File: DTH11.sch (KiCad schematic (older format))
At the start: 2 parts, among them P7 CONN_01X03

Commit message: finalizado enrutado provisional
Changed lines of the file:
@@
 $Descr User 8268 5846
 encoding utf-8
-Sheet 14 14
+Sheet 14 15
 Title ""
 Date ""
@@
 $EndDescr
 $Comp
-L +5V #PWR057
+L +5V #PWR050
 U 1 1 57993E23
 P 2150 1850
-F 0 "#PWR057" H 2150 1700 50  0001 C CNN
+F 0 "#PWR050" H 2150 1700 50  0001 C CNN
 F 1 "+5V" H 2165 2023 50  0000 C CNN
 F 2 "" H 2150 1850 50  0000 C CNN
@@
 $EndComp
 $Comp
-L GND #PWR058
+L GND #PWR051
 U 1 1 57993E44
-P 2350 3000
-F 0 "#PWR058" H 2350 2750 50  0001 C CNN
-F 1 "GND" H 2355 2827 50  0000 C CNN
-F 2 "" H 2350 3000 50  0000 C CNN
-F 3 "" H 2350 3000 50  0000 C CNN
-	1    2350 3000
+P 2350 3150
+F 0 "#PWR051" H 2350 2900 50  0001 C CNN
+F 1 "GND" H 2355 2977 50  0000 C CNN
+F 2 "" H 2350 3150 50  0000 C CNN
+F 3 "" H 2350 3150 50  0000 C CNN
+	1    2350 3150
 	1    0    0    -1
 $EndComp
@@
 6F 6A 98 BE 51 A3 46 8D 1A 35 6A D4 A8 51 A3 BF 6F 6A 98 BE 51 A3 46 8D 1A 35 6A D4 A8 51 A3 BF
 6F 6A 98 BE 51 A3 46 8D 1A 35 6A D4 A8 51 A3 BF 6F FA 7F 01 6A B6 0B 1D 9C B5 4B 53 00 00 00 00
-49 45 4E 44 AE 42 60 82 B1
+49 45 4E 44 AE 42 60 82 11
 EndData
 $EndBitmap

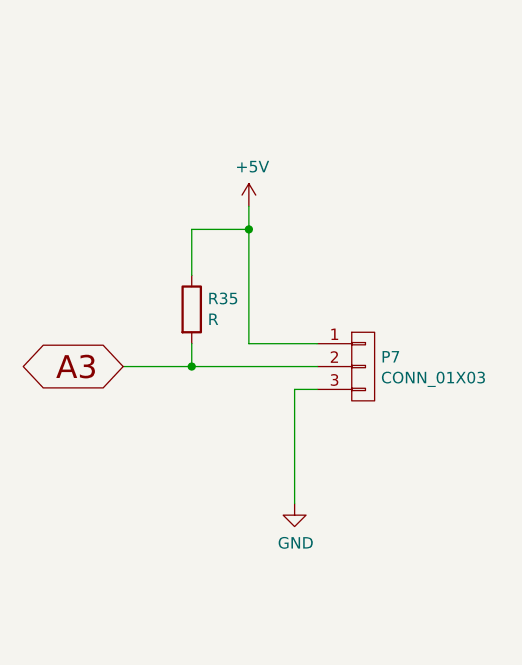
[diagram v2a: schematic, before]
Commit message: ordenar referencias de componentes
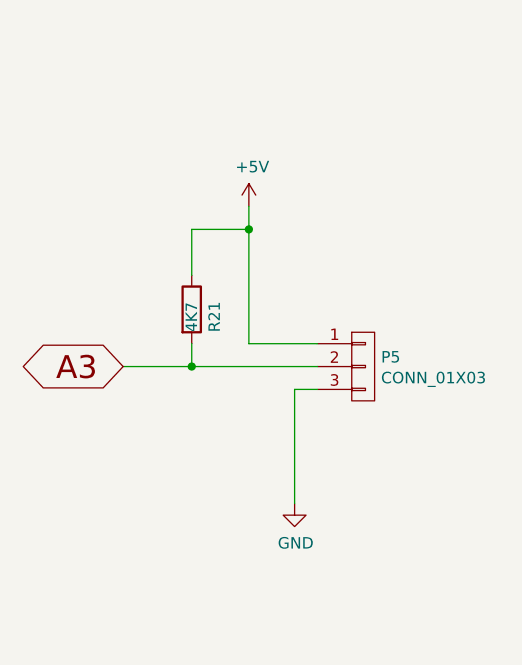
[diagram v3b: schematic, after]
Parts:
- P5: renamed from P7; Fabricante (none) -> NINIGI; Provedor (none) -> TME; Ref (none) -> ZL262-40SG; Ref_Proveedor (none) -> ZL262-40SG
- R21: renamed from R35; value R -> 4K7; Fabricante (none) -> VISHAY; Potencia (none) -> 1/8W; Provedor (none) -> TME; Ref (none) -> CRCW08054K70FKEA; Ref_Proveedor (none) -> CRCW08054K70FKEA; Tolerancia (none) -> 1%
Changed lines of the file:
@@
 $Descr User 8268 5846
 encoding utf-8
-Sheet 14 15
+Sheet 8 15
 Title ""
 Date ""
@@
 $EndDescr
 $Comp
-L +5V #PWR050
+L +5V #PWR22
 U 1 1 57993E23
 P 2150 1850
-F 0 "#PWR050" H 2150 1700 50  0001 C CNN
+F 0 "#PWR22" H 2150 1700 50  0001 C CNN
 F 1 "+5V" H 2165 2023 50  0000 C CNN
 F 2 "" H 2150 1850 50  0000 C CNN
@@
 $EndComp
 $Comp
-L GND #PWR051
+L GND #PWR23
 U 1 1 57993E44
 P 2350 3150
-F 0 "#PWR051" H 2350 2900 50  0001 C CNN
+F 0 "#PWR23" H 2350 2900 50  0001 C CNN
 F 1 "GND" H 2355 2977 50  0000 C CNN
 F 2 "" H 2350 3150 50  0000 C CNN
@@
 6F 6A 98 BE 51 A3 46 8D 1A 35 6A D4 A8 51 A3 BF 6F 6A 98 BE 51 A3 46 8D 1A 35 6A D4 A8 51 A3 BF
 6F 6A 98 BE 51 A3 46 8D 1A 35 6A D4 A8 51 A3 BF 6F FA 7F 01 6A B6 0B 1D 9C B5 4B 53 00 00 00 00
-49 45 4E 44 AE 42 60 82 11
+49 45 4E 44 AE 42 60 82 E1
 EndData
 $EndBitmap
 $Comp
-L CONN_01X03 P7
+L CONN_01X03 P5
 U 1 1 57993F2D
 P 2650 2550
-F 0 "P7" H 2728 2591 50  0000 L CNN
+F 0 "P5" H 2728 2591 50  0000 L CNN
 F 1 "CONN_01X03" H 2728 2500 50  0000 L CNN
 F 2 "Socket_Strips:Socket_Strip_Straight_1x03" H 2650 2550 50  0001 C CNN
 F 3 "" H 2650 2550 50  0000 C CNN
+F 4 "NINIGI" H 2650 2550 60  0001 C CNN "Fabricante"
+F 5 "ZL262-40SG" H 2650 2550 60  0001 C CNN "Ref"
+F 6 "~" H 2650 2550 60  0001 C CNN "Potencia"
+F 7 "~" H 2650 2550 60  0001 C CNN "Tolerancia"
+F 8 "TME" H 2650 2550 60  0001 C CNN "Provedor"
+F 9 "ZL262-40SG" H 2650 2550 60  0001 C CNN "Ref_Proveedor"
 	1    2650 2550
 	1    0    0    -1
@@
 	1900 1950 1900 2150
 $Comp
-L R R35
+L R R21
 U 1 1 57993FBE
 P 1900 2300
-F 0 "R35" H 1970 2346 50  0000 L CNN
-F 1 "R" H 1970 2255 50  0000 L CNN
+F 0 "R21" V 2000 2200 50  0000 L CNN
+F 1 "4K7" V 1900 2200 50  0000 L CNN
 F 2 "Resistors_SMD:R_0805" V 1830 2300 50  0001 C CNN
 F 3 "" H 1900 2300 50  0000 C CNN
+F 4 "VISHAY" H 1900 2300 60  0001 C CNN "Fabricante"
+F 5 "CRCW08054K70FKEA" H 1900 2300 60  0001 C CNN "Ref"
+F 6 "1/8W" H 1900 2300 60  0001 C CNN "Potencia"
+F 7 "1%" H 1900 2300 60  0001 C CNN "Tolerancia"
+F 8 "TME" H 1900 2300 60  0001 C CNN "Provedor"
+F 9 "CRCW08054K70FKEA" H 1900 2300 60  0001 C CNN "Ref_Proveedor"
 	1    1900 2300
 	1    0    0    -1

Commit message: cambiados encoder y potenciometro
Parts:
- R21: footprint Resistors_SMD:R_0805 -> Resistencias:R_0805
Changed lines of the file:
@@
 $EndDescr
 $Comp
-L +5V #PWR22
+L +5V #PWR024
 U 1 1 57993E23
 P 2150 1850
-F 0 "#PWR22" H 2150 1700 50  0001 C CNN
+F 0 "#PWR024" H 2150 1700 50  0001 C CNN
 F 1 "+5V" H 2165 2023 50  0000 C CNN
 F 2 "" H 2150 1850 50  0000 C CNN
@@
 $EndComp
 $Comp
-L GND #PWR23
+L GND #PWR025
 U 1 1 57993E44
 P 2350 3150
-F 0 "#PWR23" H 2350 2900 50  0001 C CNN
+F 0 "#PWR025" H 2350 2900 50  0001 C CNN
 F 1 "GND" H 2355 2977 50  0000 C CNN
 F 2 "" H 2350 3150 50  0000 C CNN
@@
 6F 6A 98 BE 51 A3 46 8D 1A 35 6A D4 A8 51 A3 BF 6F 6A 98 BE 51 A3 46 8D 1A 35 6A D4 A8 51 A3 BF
 6F 6A 98 BE 51 A3 46 8D 1A 35 6A D4 A8 51 A3 BF 6F FA 7F 01 6A B6 0B 1D 9C B5 4B 53 00 00 00 00
-49 45 4E 44 AE 42 60 82 91
+49 45 4E 44 AE 42 60 82 C1
 EndData
 $EndBitmap
@@
 F 0 "R21" V 2000 2200 50  0000 L CNN
 F 1 "4K7" V 1900 2200 50  0000 L CNN
-F 2 "Resistors_SMD:R_0805" V 1830 2300 50  0001 C CNN
+F 2 "Resistencias:R_0805" V 1830 2300 50  0001 C CNN
 F 3 "" H 1900 2300 50  0000 C CNN
 F 4 "VISHAY" H 1900 2300 60  0001 C CNN "Fabricante"

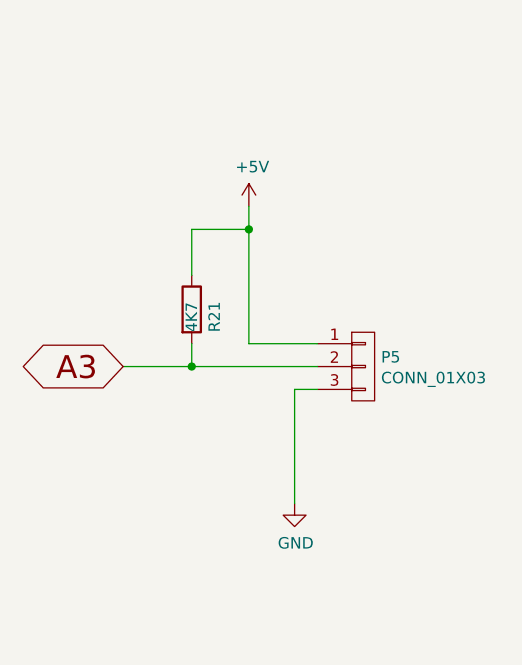
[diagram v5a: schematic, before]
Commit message: añadidos driver para led y conectores para fotodiodos infrarrojos
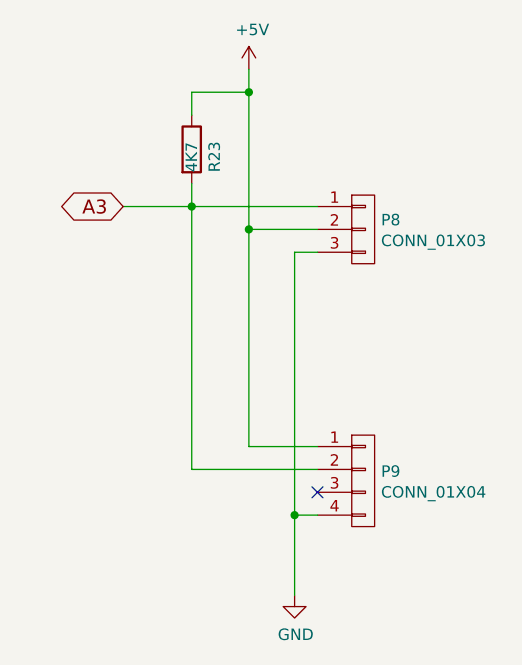
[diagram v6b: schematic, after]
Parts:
- added P9: CONN_01X04, Socket_Strips:Socket_Strip_Straight_1x04, symbol CONN_01X04
- renumbered P5 to P8, R21 to R23
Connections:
- net +5V: now also P8.2 (P2), P9.1 (P1); no longer P8.1 (P1)
- net A3: now also P8.1 (P1), P9.2 (P2); no longer P8.2 (P2)
- net GND: now also P9.4 (P4)
- no-connect marks 0 -> 1
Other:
- moved on the sheet: P8, R23
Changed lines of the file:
@@
 EESchema Schematic File Version 2
+LIBS:Interfaces
+LIBS:Nano_PB-rescue
 LIBS:Sensores
 LIBS:power
@@
 LIBS:valves
 LIBS:MyLibrary
+LIBS:matriz_led
 LIBS:Nano_PB-cache
-EELAYER 25 0
+EELAYER 26 0
 EELAYER END
 $Descr User 8268 5846
 encoding utf-8
-Sheet 8 15
+Sheet 8 16
 Title "Sensor de Temperatura y Humedad"
-Date "2016-08-07"
-Rev "V.0.2"
+Date "2017-01-04"
+Rev "V.0.3"
 Comp "NanoPlayBoard"
 Comment1 "Creada por Antonio Morales"
@@
 $EndDescr
 $Comp
-L +5V #PWR024
+L +5V #PWR045
 U 1 1 57993E23
-P 2150 1850
-F 0 "#PWR024" H 2150 1700 50  0001 C CNN
-F 1 "+5V" H 2165 2023 50  0000 C CNN
-F 2 "" H 2150 1850 50  0000 C CNN
-F 3 "" H 2150 1850 50  0000 C CNN
-	1    2150 1850
+P 2150 1250
+F 0 "#PWR045" H 2150 1100 50  0001 C CNN
+F 1 "+5V" H 2165 1423 50  0000 C CNN
+F 2 "" H 2150 1250 50  0000 C CNN
+F 3 "" H 2150 1250 50  0000 C CNN
+	1    2150 1250
 	1    0    0    -1
 $EndComp
 $Comp
-L GND #PWR025
+L GND #PWR046
 U 1 1 57993E44
-P 2350 3150
-F 0 "#PWR025" H 2350 2900 50  0001 C CNN
-F 1 "GND" H 2355 2977 50  0000 C CNN
-F 2 "" H 2350 3150 50  0000 C CNN
-F 3 "" H 2350 3150 50  0000 C CNN
-	1    2350 3150
+P 2350 3550
+F 0 "#PWR046" H 2350 3300 50  0001 C CNN
+F 1 "GND" H 2355 3377 50  0000 C CNN
+F 2 "" H 2350 3550 50  0000 C CNN
+F 3 "" H 2350 3550 50  0000 C CNN
+	1    2350 3550
 	1    0    0    -1
 $EndComp
-Text GLabel 1600 2550 0    100  BiDi ~ 0
+Text GLabel 1600 1850 0    61   BiDi ~ 0
 A3
 $Bitmap
-Pos 5550 2700
+Pos 5600 3200
 Scale 1,000000
 Data
@@
 6F 6A 98 BE 51 A3 46 8D 1A 35 6A D4 A8 51 A3 BF 6F 6A 98 BE 51 A3 46 8D 1A 35 6A D4 A8 51 A3 BF
 6F 6A 98 BE 51 A3 46 8D 1A 35 6A D4 A8 51 A3 BF 6F FA 7F 01 6A B6 0B 1D 9C B5 4B 53 00 00 00 00
-49 45 4E 44 AE 42 60 82 C1
+49 45 4E 44 AE 42 60 82
 EndData
 $EndBitmap
 $Comp
-L CONN_01X03 P5
+L CONN_01X03 P8
 U 1 1 57993F2D
-P 2650 2550
-F 0 "P5" H 2728 2591 50  0000 L CNN
-F 1 "CONN_01X03" H 2728 2500 50  0000 L CNN
-F 2 "Socket_Strips:Socket_Strip_Straight_1x03" H 2650 2550 50  0001 C CNN
-F 3 "" H 2650 2550 50  0000 C CNN
-F 4 "NINIGI" H 2650 2550 60  0001 C CNN "Fabricante"
-F 5 "ZL262-40SG" H 2650 2550 60  0001 C CNN "Ref"
-F 6 "~" H 2650 2550 60  0001 C CNN "Potencia"
-F 7 "~" H 2650 2550 60  0001 C CNN "Tolerancia"
-F 8 "TME" H 2650 2550 60  0001 C CNN "Provedor"
-F 9 "ZL262-40SG" H 2650 2550 60  0001 C CNN "Ref_Proveedor"
-	1    2650 2550
+P 2650 1950
+F 0 "P8" H 2728 1991 50  0000 L CNN
+F 1 "CONN_01X03" H 2728 1900 50  0000 L CNN
+F 2 "Socket_Strips:Socket_Strip_Straight_1x03" H 2650 1950 50  0001 C CNN
+F 3 "" H 2650 1950 50  0000 C CNN
+F 4 "NINIGI" H 2650 1950 60  0001 C CNN "Fabricante"
+F 5 "ZL262-40SG" H 2650 1950 60  0001 C CNN "Ref"
+F 6 "~" H 2650 1950 60  0001 C CNN "Potencia"
+F 7 "~" H 2650 1950 60  0001 C CNN "Tolerancia"
+F 8 "TME" H 2650 1950 60  0001 C CNN "Provedor"
+F 9 "ZL262-40SG" H 2650 1950 60  0001 C CNN "Ref_Proveedor"
+	1    2650 1950
 	1    0    0    -1
 $EndComp
-Connection ~ 1900 2550
 Wire Wire Line
-	1900 2450 1900 2550
+	1900 1750 1900 3000
 Wire Wire Line
-	1900 1950 1900 2150
+	1900 1350 1900 1450
 $Comp
-L R R21
+L R R23
 U 1 1 57993FBE
-P 1900 2300
-F 0 "R21" V 2000 2200 50  0000 L CNN
-F 1 "4K7" V 1900 2200 50  0000 L CNN
-F 2 "Resistencias:R_0805" V 1830 2300 50  0001 C CNN
-F 3 "" H 1900 2300 50  0000 C CNN
-F 4 "VISHAY" H 1900 2300 60  0001 C CNN "Fabricante"
-F 5 "CRCW08054K70FKEA" H 1900 2300 60  0001 C CNN "Ref"
-F 6 "1/8W" H 1900 2300 60  0001 C CNN "Potencia"
-F 7 "1%" H 1900 2300 60  0001 C CNN "Tolerancia"
-F 8 "TME" H 1900 2300 60  0001 C CNN "Provedor"
-F 9 "CRCW08054K70FKEA" H 1900 2300 60  0001 C CNN "Ref_Proveedor"
-	1    1900 2300
+P 1900 1600
+F 0 "R23" V 2000 1500 50  0000 L CNN
+F 1 "4K7" V 1900 1500 50  0000 L CNN
+F 2 "Resistencias:R_0805" V 1830 1600 50  0001 C CNN
+F 3 "" H 1900 1600 50  0000 C CNN
+F 4 "VISHAY" H 1900 1600 60  0001 C CNN "Fabricante"
+F 5 "CRCW08054K70FKEA" H 1900 1600 60  0001 C CNN "Ref"
+F 6 "1/8W" H 1900 1600 60  0001 C CNN "Potencia"
+F 7 "1%" H 1900 1600 60  0001 C CNN "Tolerancia"
+F 8 "TME" H 1900 1600 60  0001 C CNN "Provedor"
+F 9 "CRCW08054K70FKEA" H 1900 1600 60  0001 C CNN "Ref_Proveedor"
+	1    1900 1600
 	1    0    0    -1
 $EndComp
 Wire Wire Line
-	1600 2550 2450 2550
+	2350 2050 2350 3550
 Wire Wire Line
-	2350 2650 2350 3150
+	2450 2050 2350 2050
 Wire Wire Line
-	2450 2650 2350 2650
+	2150 1250 2150 2900
 Wire Wire Line
-	2150 2450 2450 2450
-Wire Wire Line
-	2150 1850 2150 2450
-Wire Wire Line
-	1900 1950 2150 1950
-Connection ~ 2150 1950
+	1900 1350 2150 1350
+Connection ~ 2150 1350
 $Bitmap
 Pos 7500 4400
@@
 50 17 92 01 51 92 64 0C CE 27 7B 4E 87 A3 FC C9 E9 39 BC D0 3B DC 1F CF E6 3C 60 30 83 10 3D 18
 F4 0B 89 52 73 00 8B 80 91 08 28 22 8F 6D AB AA BD D3 E7 C4 3E A7 59 B4 A9 94 4D 1C A1 84 52 AC
-9A 46 F6 7A E1 FF 00 F0 A4 0C 74 26 CB 7B D1 00 00 00 00 49 45 4E 44 AE 42 60 82 00
+9A 46 F6 7A E1 FF 00 F0 A4 0C 74 26 CB 7B D1 00 00 00 00 49 45 4E 44 AE 42 60 82
 EndData
 $EndBitmap
+$Comp
+L CONN_01X04 P9
+U 1 1 586D7C99
+P 2650 3050
+F 0 "P9" H 2728 3091 50  0000 L CNN
+F 1 "CONN_01X04" H 2728 3000 50  0000 L CNN
+F 2 "Socket_Strips:Socket_Strip_Straight_1x04" H 2650 3050 50  0001 C CNN
+F 3 "" H 2650 3050 50  0000 C CNN
+	1    2650 3050
+	1    0    0    -1
+$EndComp
+Wire Wire Line
+	2450 3200 2350 3200
+Connection ~ 2350 3200
+Wire Wire Line
+	2150 2900 2450 2900
+Wire Wire Line
+	1900 3000 2450 3000
+NoConn ~ 2450 3100
+Wire Wire Line
+	2450 1950 2150 1950
+Connection ~ 2150 1950
+Wire Wire Line
+	1600 1850 2450 1850
+Connection ~ 1900 1850
 $EndSCHEMATC

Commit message: Se añade un expansor GPIO al esquema y se elminan registros y codificador
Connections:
- net A3 renamed D12
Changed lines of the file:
@@
 LIBS:MyLibrary
 LIBS:matriz_led
+LIBS:Pasivos
 LIBS:Nano_PB-cache
 EELAYER 26 0
@@
 $Descr User 8268 5846
 encoding utf-8
-Sheet 8 16
+Sheet 9 17
 Title "Sensor de Temperatura y Humedad"
-Date "2017-01-04"
-Rev "V.0.3"
+Date "2017-01-19"
+Rev "V.0.4"
 Comp "NanoPlayBoard"
 Comment1 "Creada por Antonio Morales"
@@
 $EndDescr
 $Comp
-L +5V #PWR044
+L +5V #PWR046
 U 1 1 57993E23
 P 2150 1250
-F 0 "#PWR044" H 2150 1100 50  0001 C CNN
+F 0 "#PWR046" H 2150 1100 50  0001 C CNN
 F 1 "+5V" H 2165 1423 50  0000 C CNN
 F 2 "" H 2150 1250 50  0000 C CNN
@@
 $EndComp
 $Comp
-L GND #PWR045
+L GND #PWR047
 U 1 1 57993E44
 P 2350 3550
-F 0 "#PWR045" H 2350 3300 50  0001 C CNN
+F 0 "#PWR047" H 2350 3300 50  0001 C CNN
 F 1 "GND" H 2355 3377 50  0000 C CNN
 F 2 "" H 2350 3550 50  0000 C CNN
@@
 $EndComp
 Text GLabel 1600 1850 0    61   BiDi ~ 0
-A3
+D12
 $Bitmap
 Pos 5600 3200
